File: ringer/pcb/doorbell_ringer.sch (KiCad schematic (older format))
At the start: 9 parts, among them Q1 MMBT3904, U1 ESP32-WROOM-32

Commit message: Microphone Circuit
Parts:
- removed Q1: MMBT3904, Package_TO_SOT_SMD:SOT-23, symbol Transistor_BJT:MMBT3904
- removed U1: ESP32-WROOM-32, RF_Module:ESP32-WROOM-32, symbol RF_Module:ESP32-WROOM-32
- added C4: 2.2u, symbol Device:C
- added R4, R6: 100k, symbol Device:R
- added R5: 47, symbol Device:R
- added U2: TL074, symbol Amplifier_Operational:TL074
- added U?: ESP32-WROOM-32, RF_Module:ESP32-WROOM-32, symbol RF_Module:ESP32-WROOM-32
- C1, C2: value 100n -> 2.2u
- C3: value 100n -> 15p
- MK1: value Microphone_Condenser -> Electret Microphone
- R1: value 10k -> 2.2k; footprint Resistor_SMD:R_0805_2012Metric -> (none)
- R2: value 100k -> 75k; footprint Resistor_SMD:R_0805_2012Metric -> (none)
- R3: value 10k -> 100k; footprint Resistor_SMD:R_0805_2012Metric -> (none)
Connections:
- net labels added: mic
- net labels removed: Microphone
- wire segments 25 -> 29
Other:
- note added: "C1 should be big enough\nto have an impedance\nmuch lower than R1"
- note added: "TODO\nDecoupling capacitors"
- note removed: "Decoupling Capacitors"

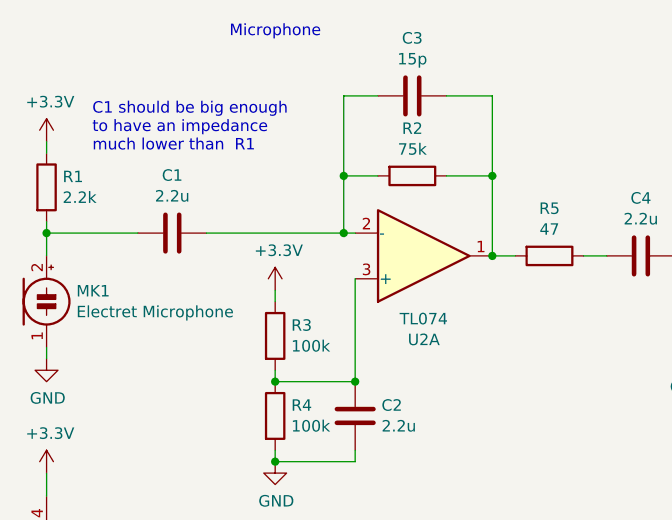
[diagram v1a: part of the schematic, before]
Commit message: Mic Pre Amp
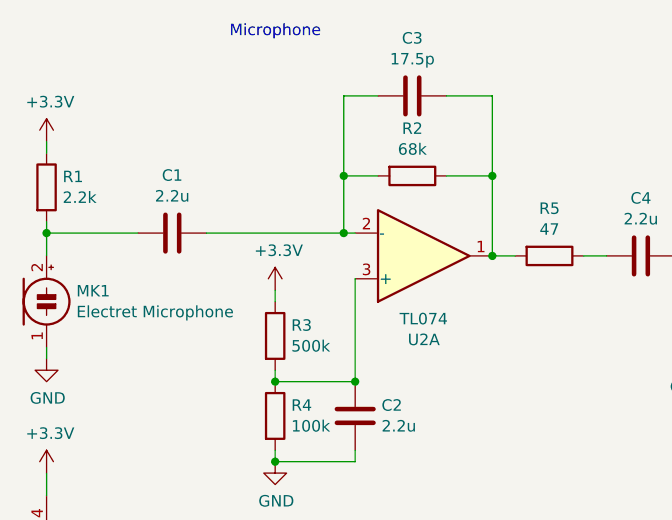
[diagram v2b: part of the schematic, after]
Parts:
- C3: value 15p -> 17.5p
- R2: value 75k -> 68k
- R3: value 100k -> 500k
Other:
- note removed: "C1 should be big enough\nto have an impedance\nmuch lower than R1"

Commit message: Mic Pre amp
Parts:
- removed C1, C2, C4: 2.2u, symbol Device:C
- removed C3: 17.5p, symbol Device:C
- removed MK1: Electret Microphone, symbol Device:Microphone_Condenser
- removed R1: 2.2k, symbol Device:R
- removed R2: 68k, symbol Device:R
- removed R3: 500k, symbol Device:R
- removed R4, R6: 100k, symbol Device:R
- removed R5: 47, symbol Device:R
- removed U2: TL074, symbol Amplifier_Operational:TL074
- added C? (x2): 100n, symbol Device:C
- added MK?: Microphone_Condenser, symbol Device:Microphone_Condenser
- added Q?: 2N2219, Package_TO_SOT_THT:TO-39-3, symbol Transistor_BJT:2N2219
- added R? (x2): 10k, symbol Device:R
- added R?: 100k, symbol Device:R
- added R? (x2): 1k, symbol Device:R
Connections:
- net +3V3: now also R?.1, R?.1, R?.2
- net GND: now also MK?.1 (-), Q?.1 (E), R?.2
- net mic: now also C?.1, R?.1, R?.2
- new net: C?.1, Q?.2 (B), R?.2
- new net: C?.2, Q?.3 (C), R?.1, R?.2
- new net: C?.2, MK?.2 (+), R?.1
